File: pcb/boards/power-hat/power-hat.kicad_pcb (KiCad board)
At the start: 2 copper layers, 65 x 56 mm, 48 parts, among them J1 ISO_A, J2 Raspberry_Pi_GPIO, J3 ISP, J4 FAN_4PIN, Q1 IRLB8721PBF, Q2 2N7002, Q3 2N7002, U1 TPS54560BDDA, U2 LTV-817S, U3 attiny85, Y1 16Mhz Crystal

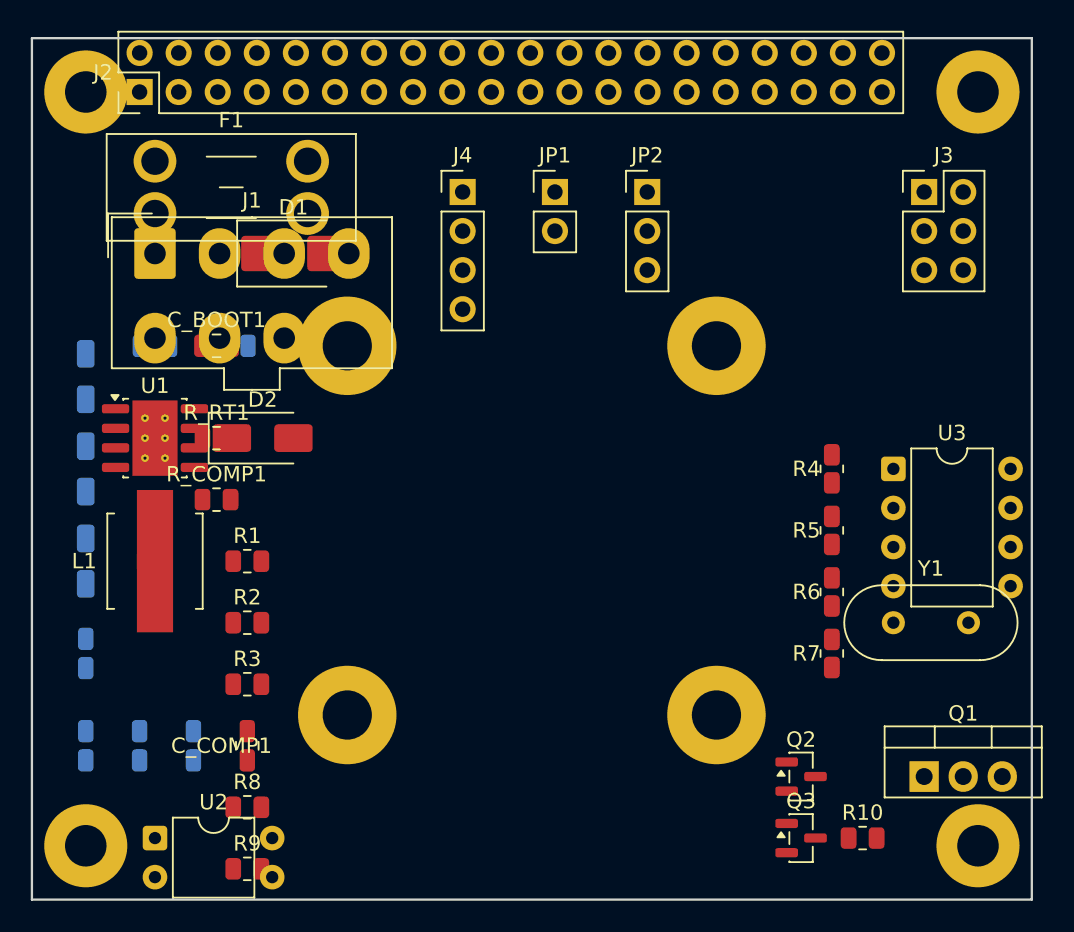
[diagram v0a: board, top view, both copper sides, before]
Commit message: Power HAT PCB: Move SMD components to back layer for optimized layout
- Moved 16 SMD components to B.Cu (back layer):
  - 12 resistors: R1-R10, R_RT1, R_COMP1
  - 2 diodes: D1 (SMB), D2 (SMA)
  - 2 MOSFETs: Q2, Q3 (SOT-23 gate drivers)

- Strategic positioning under related front-layer components:
  - Buck converter passives under U1
  - MCU resistors under U3
  - Opto resistors under U2
  - Gate driver circuit under Q1
  - Input protection under J1

- Added layout scripts:
  - move_smd_to_back.py: Flip components to back layer
  - fix_back_positions.py: Apply board offset correction

- Updated documentation with two-layer component strategy

Co-Authored-By: Claude Opus 4.5 <noreply@anthropic.com>
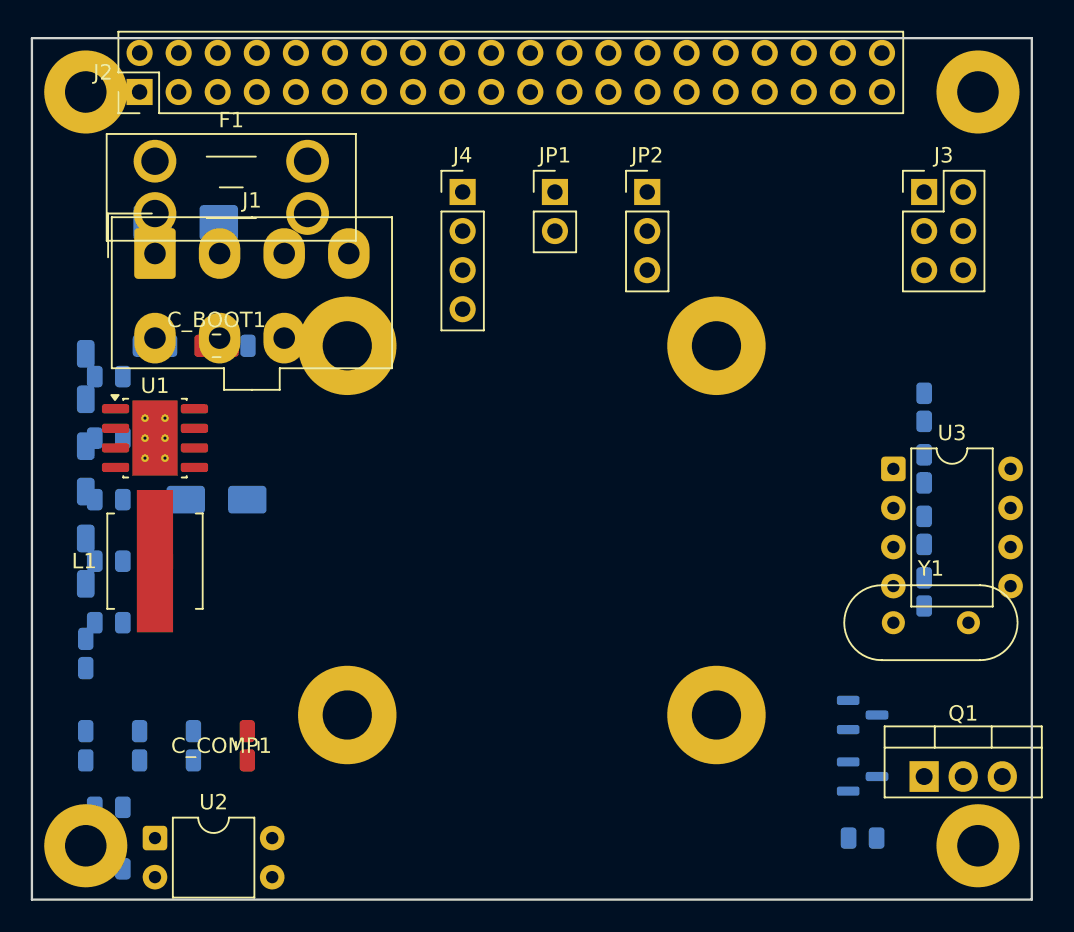
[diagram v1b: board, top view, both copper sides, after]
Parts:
- D1, D2, Q2, Q3, R1, R10, R2, R3, R4, R5, R6, R7, R8, R9, R_COMP1, R_RT1: moved to B.Cu
- moved R1 9.85 mm to (100.8, 84.0)
- moved R2 9.85 mm to (100.8, 88.0)
- moved R3 9.85 mm to (100.8, 92.0)
- moved R8 9.00 mm to (100.8, 104.0)
- moved R9 9.00 mm to (100.8, 108.0)
- moved R_COMP1 8.06 mm to (100.8, 80.0)
- moved R_RT1 8.06 mm to (100.8, 76.0)
- moved D1 7.28 mm to (105.8, 66.0)
- moved R4 7.21 mm to (153.8, 78.0)
- moved R5 7.21 mm to (153.8, 82.0)
- moved R6 7.21 mm to (153.8, 86.0)
- moved R7 7.21 mm to (153.8, 90.0)
- moved Q2 5.66 mm to (149.8, 98.0)
- moved Q3 5.66 mm to (149.8, 102.0)
- moved D2 5.00 mm to (107.8, 84.0)

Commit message: Power HAT: Fix ERC errors - 0 errors, 55 warnings
Manual schematic fixes:
- J1: Updated to Molex Micro-Fit 3.0 6-pin connector
- C6: Fixed short - changed bottom pin from +3.3V to GND
- C8: Reconnected as feedforward cap (+5V to U1-FB)
- C9: Fixed net label from 12V_IGN to 12V_FUSED
- R6: Fixed label to 12V_IGN to GND (ignition divider)
- D1 (TVS): Moved away from J2, reconnected 12V_FUSED to GND
- Removed stray 12V_IGN label hidden behind U1
- Added PWR_FLAG to 12V_FUSED and +3.3V nets

All critical ERC errors resolved. Remaining 55 warnings are
non-critical (off-grid endpoints, dangling labels, same local/global).

Co-Authored-By: Claude Opus 4.5 <noreply@anthropic.com>
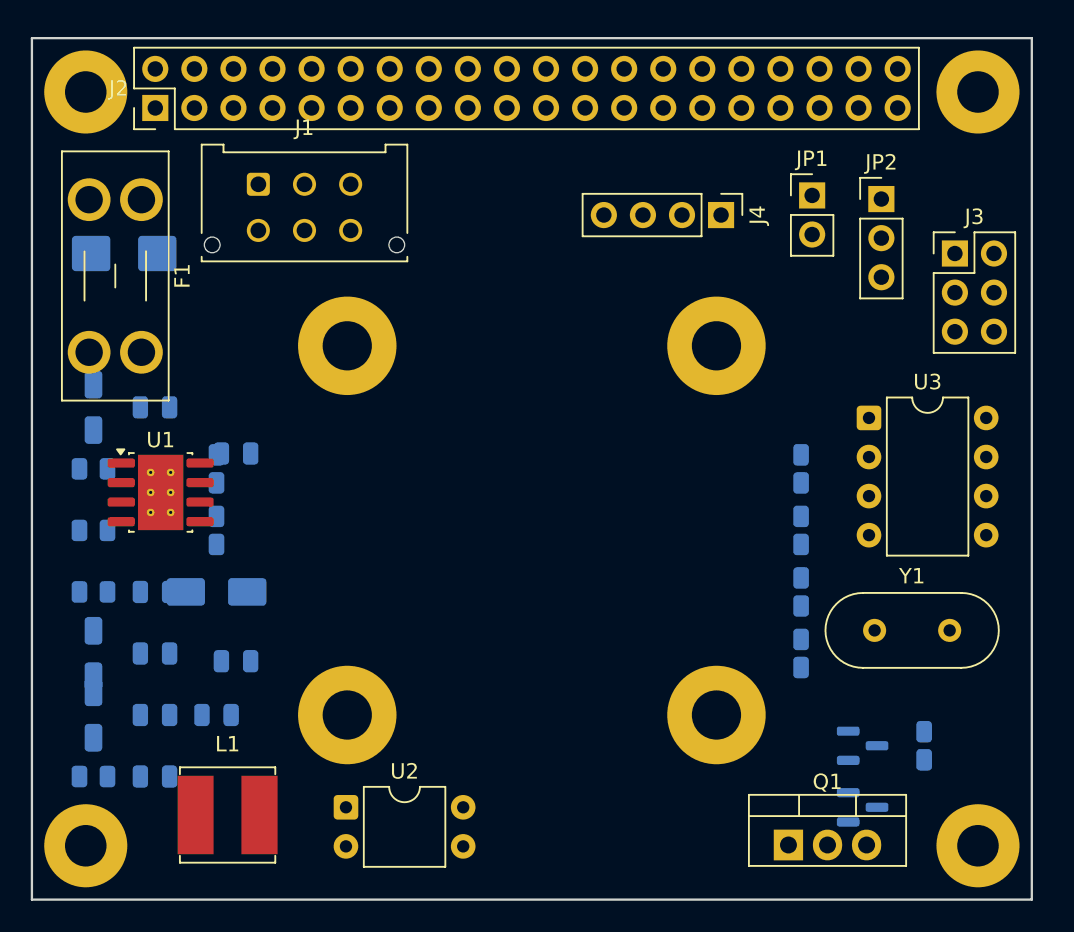
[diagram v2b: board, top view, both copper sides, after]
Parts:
- C8: value 10uF -> 47pF
- C_BOOT1, C_COMP1: moved to B.Cu
- J1: value ISO_A -> Micro-Fit_3.0; footprint Connector_Molex:Molex_Mini-Fit_Jr_5566-08A_2x04_P4.20mm_Vertical -> Connector_Molex:Molex_Micro-Fit_3.0_43045-0612_2x03_P3.00mm_Vertical
- moved C3 17.5 mm to (103.8, 90.0)
- moved L1 17.2 mm to (108.5, 104.5), turned to 0 degrees
- moved J4 16.9 mm to (140.6, 65.5), turned to -90 degrees
- moved JP1 16.7 mm to (146.5, 64.2)
- moved JP2 15.2 mm to (151.0, 64.5)
- moved U2 12.6 mm to (116.2, 104.0)
- moved C8 12.0 mm to (99.8, 94.0)
- moved C9 10.0 mm to (99.8, 98.0)
- moved Q1 9.88 mm to (145.0, 106.5)
- moved C5 9.39 mm to (107.8, 98.0), turned to 0 degrees
- moved R4 8.94 mm to (145.8, 82.0)
- moved R5 8.94 mm to (145.8, 86.0)
- moved R6 8.94 mm to (145.8, 90.0)
- moved R7 8.94 mm to (145.8, 94.0)
- moved J1 8.09 mm to (110.5, 63.5)
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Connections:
- C6 pad 2: +3.3V -> GND
- C8 pad 1: XTAL2 -> +5V
- C8 pad 2: GND -> U1-FB
- D2 pad 2: 12V_FUSED -> 12V_IGN
- F1 pad 1: 12V_FUSED -> 12V_IGN
- J1 pad 1: 12V_FUSED -> 12V_IGN
- J1 pad 2: 12V_ACC -> 12V_IGN
- J1 pad 3: 12V_FUSED -> 12V_ACC
- J1 pad 4: 12V_FUSED -> GND
- J2 pad 1: +3.3V -> 12V_FUSED
- R6 pad 1: 12V_FUSED -> 12V_IGN
- U1 pad 3: 12V_FUSED -> 12V_IGN

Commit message: Power HAT PCB: DRC clean routing via FreeRouting
- Complete auto-routing with FreeRouting (power-hat.ses)
- All DRC errors resolved (120 warnings, 0 errors)
- Fixed J2 +5V/GND short, edge clearance, R_COMP1 clearance
- Added keepout zone for fan cutout area
- Added STATUS.md with next steps (power trace widths need widening)

TODO: Widen power traces (12V_FUSED, +5V, GND, U1_SW) from 0.2mm to 1.5mm

Co-Authored-By: Claude Opus 4.5 <noreply@anthropic.com>
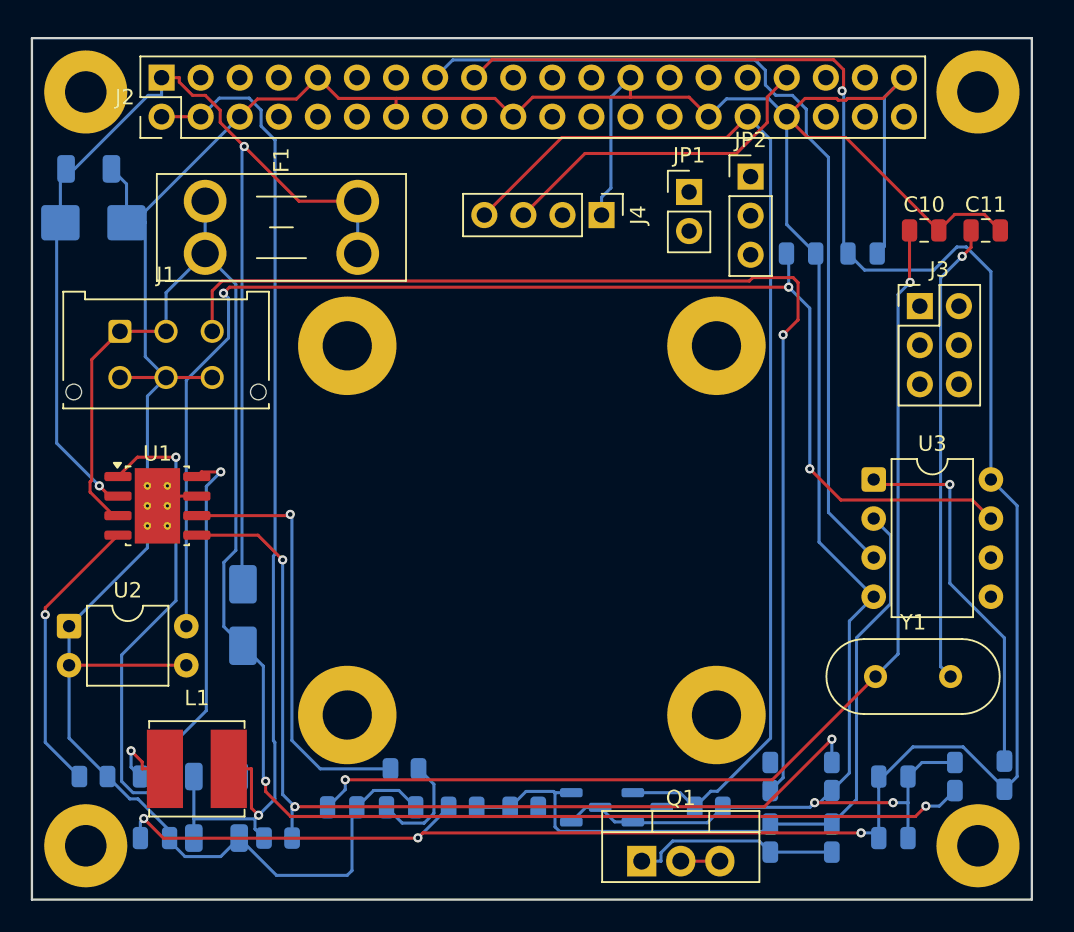
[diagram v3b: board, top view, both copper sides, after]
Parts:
- added C10: 22pF, Capacitor_SMD:C_0805_2012Metric, F.Cu at (153.8, 66.5)
- added C11: 22pF, Capacitor_SMD:C_0805_2012Metric, F.Cu at (157.8, 66.5)
- moved C4 52.8 mm to (149.8, 68.0)
- moved C6 48.7 mm to (151.8, 106.0)
- moved C3 47.4 mm to (145.8, 68.0)
- moved R1 44.7 mm to (147.8, 102.0)
- moved R2 44.7 mm to (147.8, 106.0)
- moved C5 44.2 mm to (151.8, 102.0)
- moved C9 35.5 mm to (99.5, 62.5), turned to 0 degrees
- moved C2 29.1 mm to (107.8, 106.0), turned to 0 degrees
- moved R9 28.1 mm to (127.8, 104.0)
- moved C1 28.0 mm to (103.8, 106.0)
- moved R_COMP1 25.5 mm to (120.0, 101.5)
- moved R8 24.1 mm to (123.8, 104.0)
- moved C_BOOT1 21.7 mm to (103.8, 102.0)
- moved U2 21.5 mm to (98.2, 92.2)
- moved R4 20.1 mm to (143.8, 102.0)
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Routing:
- net GND: track 0.00 -> 274.1 mm, vias 0 -> 2
- net +3.3V: track 0.00 -> 149.9 mm, vias 0 -> 4
- net 12V_IGN: track 0.00 -> 109.6 mm, vias 0 -> 2
- net IGN_DETECT: track 0.00 -> 87.6 mm, vias 0 -> 3
- net 12V_FUSED: track 0.00 -> 81.5 mm, vias 0 -> 2
- net 12V_ACC: track 0.00 -> 75.0 mm, vias 0 -> 1
- net FAN_PWM: track 0.00 -> 72.0 mm
- net XTAL1: track 0.00 -> 69.5 mm, vias 0 -> 2
- net +5V: track 0.00 -> 68.5 mm, vias 0 -> 1
- net /U1_FB: track 0.00 -> 63.0 mm, vias 0 -> 3
- net SHUTDOWN_REQ: track 0.00 -> 57.5 mm
- net GATE_CTRL: track 0.00 -> 49.0 mm
- net /U1_BOOT: track 0.00 -> 30.7 mm, vias 0 -> 1
- net XTAL2: track 0.00 -> 30.1 mm, vias 0 -> 1
- net /U1_SW: track 0.00 -> 28.5 mm, vias 0 -> 2
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
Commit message: DAC/Amp HAT: Configure net classes and complete +12V routing
- Add net classes for power traces (+12V, Speaker, +3.3V, +5V)
- Route +12V to TPA3116D2 amplifier ICs (U3, U4)
- Fix clearance violations by setting +12V clearance to 0.2mm
- DRC: 19 warnings (cosmetic), 0 unconnected pads
- Power HAT: Include updated routing files

Co-Authored-By: Claude Opus 4.5 <noreply@anthropic.com>
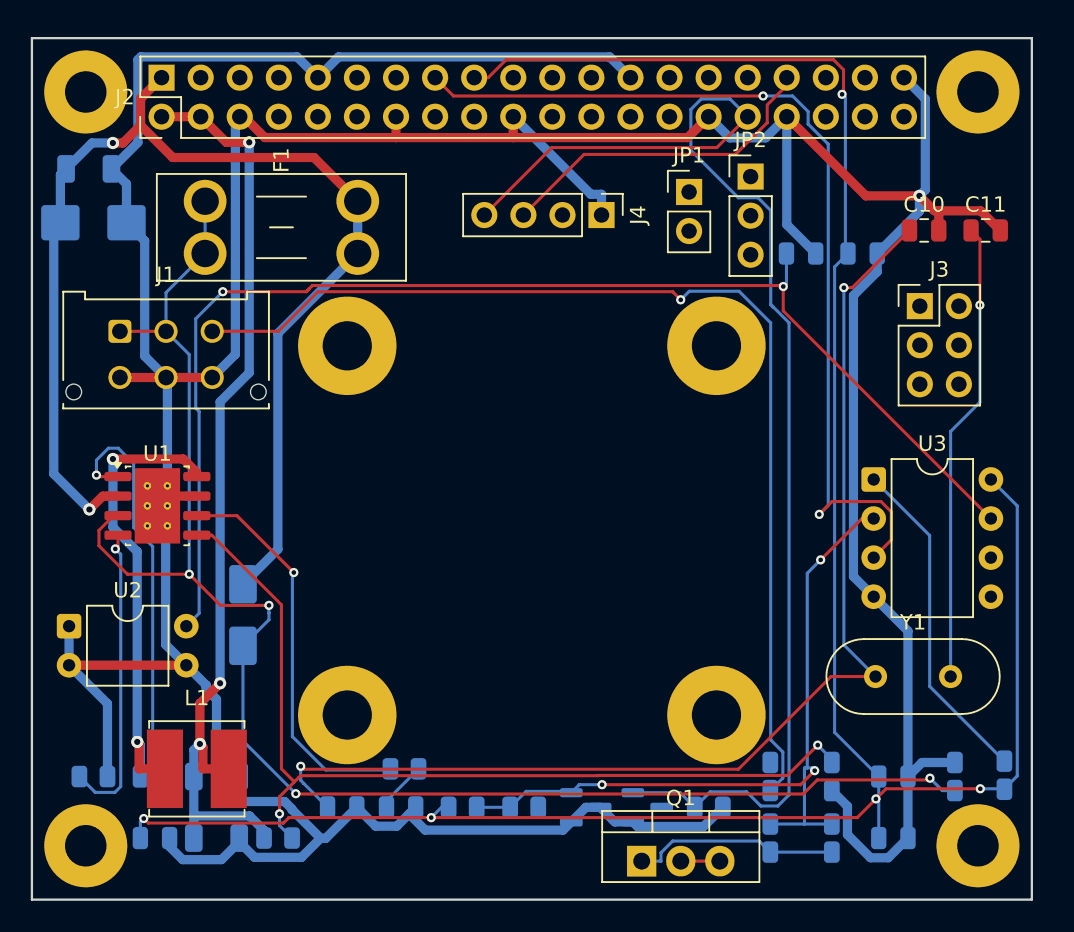
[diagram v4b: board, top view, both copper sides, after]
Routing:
- net GND: track 274.1 -> 327.4 mm, vias 2 -> 1
- net FAN_PWM: track 72.0 -> 84.0 mm
- net +3.3V: track 149.9 -> 157.6 mm, vias 4 -> 5
- net 12V_IGN: track 109.6 -> 102.7 mm, vias 2 -> 4
- net +5V: track 68.5 -> 61.9 mm, vias 1 -> 3
- net XTAL1: track 69.5 -> 75.3 mm
- net 12V_ACC: track 75.0 -> 69.7 mm
- net IGN_DETECT: track 87.6 -> 82.7 mm, vias 3 -> 2
- net /U1_BOOT: track 30.7 -> 26.9 mm
- net /COMP_RC: track 7.07 -> 3.36 mm
- net SHUTDOWN_REQ: track 57.5 -> 60.9 mm, vias 0 -> 2
- net /U1_FB: track 63.0 -> 60.1 mm, vias 3 -> 2
- net RESET: track 24.5 -> 21.8 mm, vias 1 -> 0
- net /U1_SW: track 28.5 -> 30.9 mm
- net /U1_COMP: track 28.0 -> 25.8 mm
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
